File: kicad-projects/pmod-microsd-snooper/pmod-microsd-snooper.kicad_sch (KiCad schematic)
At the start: 7 parts, among them J1 PMOD_Host_Conn_02x06, J3 Micro_SD_Card_Det2, J4 PMOD_Peripheral_Conn_02x06

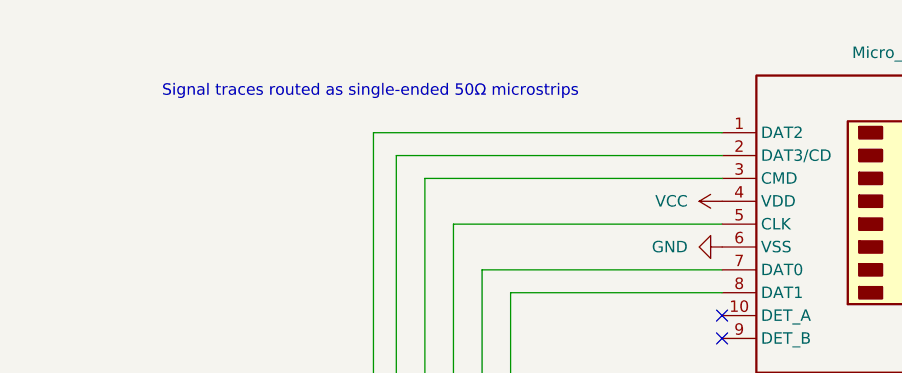
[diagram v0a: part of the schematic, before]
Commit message: Remove outdated comment
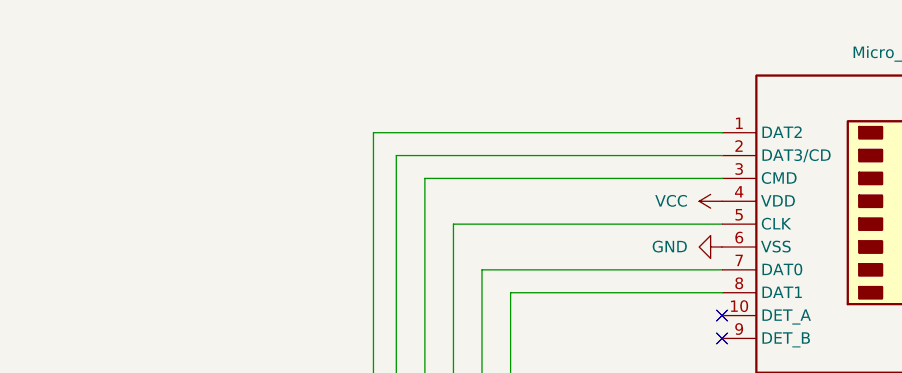
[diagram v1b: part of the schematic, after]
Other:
- note removed: "Signal traces routed as single-ended 50Ω microstrips"
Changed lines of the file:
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@@
     (stroke (width 0) (type default))
-  )
-  (text "Signal traces routed as single-ended 50Ω microstrips"
-    (at 76.835 57.785 0)
-    (effects (font (size 1.27 1.27)) (justify left bottom))
   )
   (text "SD card decoupling" (at 193.675 56.515 0)
@@
     (pin "9")
     (instances
-      (project "pmod-microsd-socket"
+      (project "pmod-microsd-snooper"
         (path "/3e223295-1bcd-481b-890e-ced5dbc15ca3"
           (reference "J1") (unit 1)
@@
     (pin "1")
     (instances
-      (project "pmod-microsd-socket"
+      (project "pmod-microsd-snooper"
         (path "/3e223295-1bcd-481b-890e-ced5dbc15ca3"
           (reference "#PWR013") (unit 1)
@@
     (pin "1")
     (instances
-      (project "pmod-microsd-socket"
+      (project "pmod-microsd-snooper"
         (path "/3e223295-1bcd-481b-890e-ced5dbc15ca3"
           (reference "#PWR012") (unit 1)
@@
     (pin "1")
     (instances
-      (project "pmod-microsd-socket"
+      (project "pmod-microsd-snooper"
         (path "/3e223295-1bcd-481b-890e-ced5dbc15ca3"
           (reference "#PWR05") (unit 1)
@@
     (pin "1")
     (instances
-      (project "pmod-microsd-socket"
+      (project "pmod-microsd-snooper"
         (path "/3e223295-1bcd-481b-890e-ced5dbc15ca3"
           (reference "#PWR017") (unit 1)
@@
     (pin "1")
     (instances
-      (project "pmod-microsd-socket"
+      (project "pmod-microsd-snooper"
         (path "/3e223295-1bcd-481b-890e-ced5dbc15ca3"
           (reference "#PWR01") (unit 1)
@@
     (pin "2")
     (instances
-      (project "pmod-microsd-socket"
+      (project "pmod-microsd-snooper"
         (path "/3e223295-1bcd-481b-890e-ced5dbc15ca3"
           (reference "C1") (unit 1)
@@
     (pin "2")
     (instances
-      (project "pmod-microsd-socket"
+      (project "pmod-microsd-snooper"
         (path "/3e223295-1bcd-481b-890e-ced5dbc15ca3"
           (reference "C3") (unit 1)
@@
     (pin "1")
     (instances
-      (project "pmod-microsd-socket"
+      (project "pmod-microsd-snooper"
         (path "/3e223295-1bcd-481b-890e-ced5dbc15ca3"
           (reference "#PWR09") (unit 1)
@@
     (pin "1")
     (instances
-      (project "pmod-microsd-socket"
+      (project "pmod-microsd-snooper"
         (path "/3e223295-1bcd-481b-890e-ced5dbc15ca3"
           (reference "#PWR014") (unit 1)
@@
     (pin "1")
     (instances
-      (project "pmod-microsd-socket"
+      (project "pmod-microsd-snooper"
         (path "/3e223295-1bcd-481b-890e-ced5dbc15ca3"
           (reference "#PWR06") (unit 1)
@@
     (pin "1")
     (instances
-      (project "pmod-microsd-socket"
+      (project "pmod-microsd-snooper"
         (path "/3e223295-1bcd-481b-890e-ced5dbc15ca3"
           (reference "#PWR015") (unit 1)
@@
     (pin "1")
     (instances
-      (project "pmod-microsd-socket"
+      (project "pmod-microsd-snooper"
         (path "/3e223295-1bcd-481b-890e-ced5dbc15ca3"
           (reference "#PWR08") (unit 1)
@@
     (pin "1")
     (instances
-      (project "pmod-microsd-socket"
+      (project "pmod-microsd-snooper"
         (path "/3e223295-1bcd-481b-890e-ced5dbc15ca3"
           (reference "#PWR010") (unit 1)
@@
     (pin "9")
     (instances
-      (project "pmod-microsd-socket"
+      (project "pmod-microsd-snooper"
         (path "/3e223295-1bcd-481b-890e-ced5dbc15ca3"
           (reference "J4") (unit 1)
@@
     (pin "1")
     (instances
-      (project "pmod-microsd-socket"
+      (project "pmod-microsd-snooper"
         (path "/3e223295-1bcd-481b-890e-ced5dbc15ca3"
           (reference "#PWR02") (unit 1)
@@
     (pin "1")
     (instances
-      (project "pmod-microsd-socket"
+      (project "pmod-microsd-snooper"
         (path "/3e223295-1bcd-481b-890e-ced5dbc15ca3"
           (reference "#PWR016") (unit 1)
@@
     (pin "9")
     (instances
-      (project "pmod-microsd-socket"
+      (project "pmod-microsd-snooper"
         (path "/3e223295-1bcd-481b-890e-ced5dbc15ca3"
           (reference "J3") (unit 1)
@@
     (pin "1")
     (instances
-      (project "pmod-microsd-socket"
+      (project "pmod-microsd-snooper"
         (path "/3e223295-1bcd-481b-890e-ced5dbc15ca3"
           (reference "#PWR03") (unit 1)
@@
     (pin "2")
     (instances
-      (project "pmod-microsd-socket"
+      (project "pmod-microsd-snooper"
         (path "/3e223295-1bcd-481b-890e-ced5dbc15ca3"
           (reference "C2") (unit 1)
@@
     (pin "2")
     (instances
-      (project "pmod-microsd-socket"
+      (project "pmod-microsd-snooper"
         (path "/3e223295-1bcd-481b-890e-ced5dbc15ca3"
           (reference "R1") (unit 1)
@@
     (pin "1")
     (instances
-      (project "pmod-microsd-socket"
+      (project "pmod-microsd-snooper"
         (path "/3e223295-1bcd-481b-890e-ced5dbc15ca3"
           (reference "#PWR07") (unit 1)
@@
     (pin "1")
     (instances
-      (project "pmod-microsd-socket"
+      (project "pmod-microsd-snooper"
         (path "/3e223295-1bcd-481b-890e-ced5dbc15ca3"
           (reference "#PWR04") (unit 1)
@@
     (pin "1")
     (instances
-      (project "pmod-microsd-socket"
+      (project "pmod-microsd-snooper"
         (path "/3e223295-1bcd-481b-890e-ced5dbc15ca3"
           (reference "#PWR011") (unit 1)
